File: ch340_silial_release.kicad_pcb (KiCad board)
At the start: 2 copper layers, 50 x 20 mm, 14 parts, among them J1 USB_B, J2 Conn_01x05_Pin, U1 CH340N

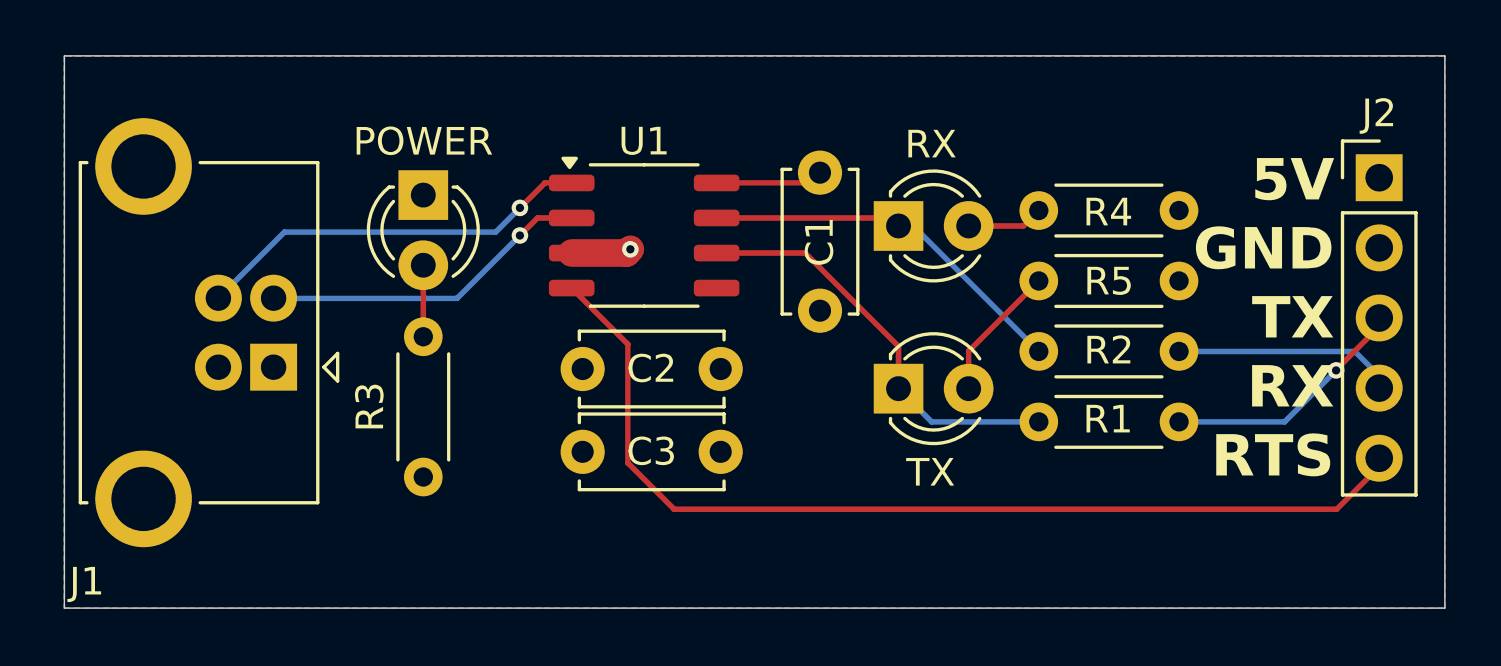
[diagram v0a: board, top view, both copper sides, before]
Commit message: フットプリント修正
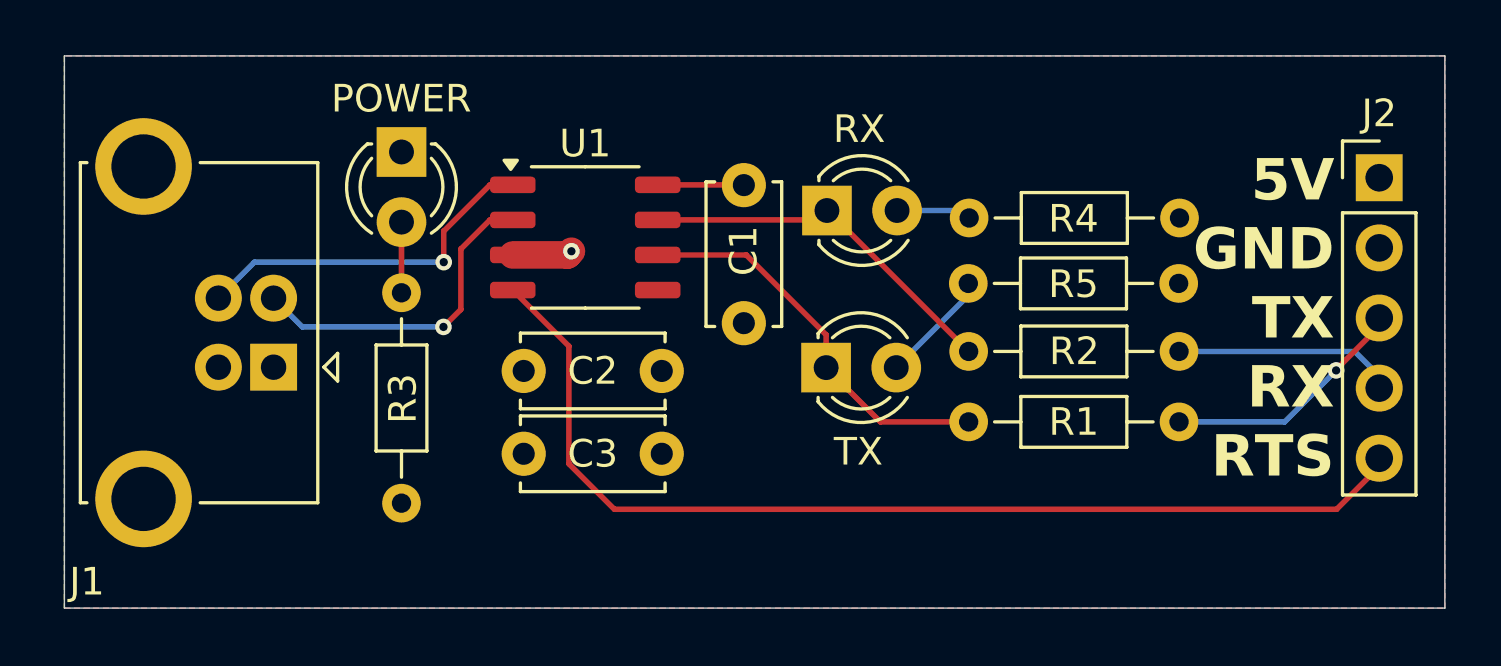
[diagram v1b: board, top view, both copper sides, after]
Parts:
- R1, R2, R3, R4, R5: footprint Resistor_THT:R_Axial_DIN0204_L3.6mm_D1.6mm_P5.08mm_Horizontal -> Resistor_THT:R_Axial_DIN0204_L3.6mm_D1.6mm_P7.62mm_Horizontal
- moved C1 2.79 mm to (124.6, 54.7)
- moved TX 2.73 mm to (127.6, 61.3)
- moved RX 2.65 mm to (127.6, 55.6)
- moved R5 2.55 mm to (132.7, 58.2)
- moved R4 2.54 mm to (132.8, 55.9)
- moved C2 2.14 mm to (121.6, 61.4)
- moved C3 2.14 mm to (121.6, 64.4)
- moved U1 2.14 mm to (118.9, 56.6)
- moved POWER 1.75 mm to (112.2, 53.5)
- moved R3 1.23 mm to (112.2, 66.2)
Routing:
- net reset: track 36.3 -> 38.3 mm
- net Net-(J1-D+): track 14.9 -> 13.2 mm
- net Net-(D2-A): track 4.95 -> 4.13 mm
- net Net-(U1-V3): track 3.90 -> 3.12 mm
- net Net-(D2-K): track 15.1 -> 14.5 mm
